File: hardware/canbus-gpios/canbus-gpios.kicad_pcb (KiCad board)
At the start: 4 copper layers, 55 x 35 mm, 34 parts, among them J1 USB_B_Micro, J2 UART, J3 10k NTC, J4 CANBus, J5 CANBus, J6 SWD, Q1 2N7002, Q2 2N7002, U1 MCP1754S-3302xCB, U2 STM32F042F6Px, U3 Voltage Regulator, U4 MCP2562HD

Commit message: Updated canbus-gpios to do GPIOs
- START_RUN and IGNITION_SENSE are active high 12V.
- EMERGENCY_STOP is active low 12V.
- all GPIOs converted to active high 3.3V at the CPU
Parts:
- added Q3: 2N7002, Package_TO_SOT_SMD:SOT-23, B.Cu at (100.4, 84.8)
- added Q4: 2N7002, Package_TO_SOT_SMD:SOT-23, B.Cu at (100.3, 81.3)
- added Q5: 2N7002, Package_TO_SOT_SMD:SOT-23, B.Cu at (100.3, 77.7)
- added R10: 10k, Resistor_SMD:R_0805_2012Metric_Pad1.20x1.40mm_HandSolder, B.Cu at (104.5, 75.0)
- added R8: 10k, Resistor_SMD:R_0805_2012Metric_Pad1.20x1.40mm_HandSolder, B.Cu at (100.9, 87.8)
- added R9: 10k, Resistor_SMD:R_0805_2012Metric_Pad1.20x1.40mm_HandSolder, B.Cu at (107.3, 80.2)
- J3: value 10k NTC -> GPIO; footprint TerminalBlock_TE-Connectivity:TerminalBlock_TE_282834-2_1x02_P2.54mm_Horizontal -> TerminalBlock_TE-Connectivity:TerminalBlock_TE_282834-3_1x03_P2.54mm_Horizontal
- R3: value 499k 1% -> 10k
- R4: value 100k 1% -> 10k
- moved R7 19.6 mm to (83.8, 81.8)
- moved R3 9.86 mm to (88.2, 81.8), turned to 90 degrees
- moved R4 6.00 mm to (86.0, 81.8), turned to 90 degrees
- moved J3 1.77 mm to (104.5, 78.8), turned to -90 degrees
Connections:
- J3 pad 1: VTHERM -> START_RUN
- J3 pad 2: GND -> IGNITION_SENSE
- R3 pad 1: +12V -> EMERGENCY_STOP_3V
- R3 pad 2: VBAT_MON -> +3V3
- R4 pad 1: VBAT_MON -> IGNITION_SENSE_3V
- R4 pad 2: GND -> +3V3
- R7 pad 1: +3V3 -> START_RUN_3V
- R7 pad 2: VTHERM -> +3V3
- U2 pad 10: ~{SPI1_SS} -> EMERGENCY_STOP_3V
- U2 pad 11: SPI1_SCK -> unconnected-(U2-Pad11)
- U2 pad 12: SPI1_MISO -> unconnected-(U2-Pad12)
- U2 pad 13: SPI1_MOSI -> unconnected-(U2-Pad13)
- U2 pad 6: VTHERM -> START_RUN_3V
- U2 pad 7: VBAT_MON -> IGNITION_SENSE_3V
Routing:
- net START_RUN_3V: track 0.00 -> 30.5 mm, vias 0 -> 2
- net +12V: track 14.4 -> 42.9 mm, vias 0 -> 1
- net VTHERM: track 25.1 -> 0.00 mm, vias 1 -> 0
- net IGNITION_SENSE_3V: track 0.00 -> 24.6 mm, vias 0 -> 2
- net EMERGENCY_STOP_3V: track 0.00 -> 18.3 mm, vias 0 -> 2
- net VBAT_MON: track 17.4 -> 0.00 mm, vias 2 -> 0
- net ~{EMERGENCY_STOP}: track 0.00 -> 8.18 mm
- net +3V3: track 22.3 -> 30.2 mm, vias 6 -> 8
- net START_RUN: track 0.00 -> 6.44 mm
- net IGNITION_SENSE: track 0.00 -> 6.07 mm
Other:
- board text added: "CANBus GPIO"
- board text removed: "CANBus Thermistor"

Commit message: Updated canbus-ds1820 board, reannotated canbus-gpios
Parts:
- renumbered J6 to J2, J2 to J3, J3 to J6, R6 to R10, R5 to R3, R3 to R4, R4 to R5, R7 to R6, R8 to R7, R9 to R8, R10 to R9
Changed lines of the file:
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@@
   (net 9 "USB_D+")
   (net 10 "unconnected-(J1-Pad4)")
-  (net 11 "Net-(J2-Pad4)")
+  (net 11 "unconnected-(J3-Pad1)")
   (net 12 "CANH")
   (net 13 "CANL")
@@
   (net 30 "SWDCLK")
   (net 31 "~{RESET}")
-  (net 32 "unconnected-(J2-Pad1)")
+  (net 32 "Net-(J3-Pad4)")
   (net 33 "START_RUN_3V")
-  (net 34 "unconnected-(J2-Pad5)")
+  (net 34 "unconnected-(J3-Pad5)")
   (net 35 "unconnected-(U3-Pad4)")
   (net 36 "/VDDA")
@@
     (property "Sheetname" "")
     (attr through_hole)
-    (fp_text reference "J6" (at 2.75 0.04 180) (layer "F.SilkS")
+    (fp_text reference "J2" (at 2.75 0.04 180) (layer "F.SilkS")
       (effects (font (size 1 1) (thickness 0.15)))
     )
@@
     (property "Sheetname" "")
     (attr smd)
-    (fp_text reference "R6" (at 2.8 0.025 180) (layer "F.SilkS")
+    (fp_text reference "R10" (at 2.8 0.025 180) (layer "F.SilkS")
       (effects (font (size 1 1) (thickness 0.15)))
     )
@@
     (property "Sheetname" "")
     (attr smd)
-    (fp_text reference "R5" (at -0.3 1.875 180) (layer "F.SilkS")
+    (fp_text reference "R3" (at -0.3 1.875 180) (layer "F.SilkS")
       (effects (font (size 1 1) (thickness 0.15)))
     )
@@
     (property "Sheetname" "")
     (attr exclude_from_pos_files)
-    (fp_text reference "J2" (at 15.11 -1.15) (layer "F.SilkS")
+    (fp_text reference "J3" (at 15.11 -1.15) (layer "F.SilkS")
       (effects (font (size 1.27 1.27) (thickness 0.127)))
     )
@@
     (fp_rect (start -1.2954 -1.3462) (end 13.97 1.3462) (layer "F.SilkS") (width 0.12) (fill none))
     (pad "1" thru_hole rect (at 0 0 270) (size 1.8796 1.8796) (drill 1.016) (layers *.Cu *.Paste *.Mask)
-      (net 32 "unconnected-(J2-Pad1)") (pinfunction "DTR") (pintype "passive+no_connect"))
+      (net 11 "unconnected-(J3-Pad1)") (pinfunction "DTR") (pintype "passive+no_connect"))
     (pad "2" thru_hole circle (at 2.54 0 270) (size 1.8796 1.8796) (drill 1.016) (layers *.Cu *.Paste *.Mask)
       (net 24 "RXD2") (pinfunction "RXD") (pintype "passive"))
@@
       (net 23 "TXD2") (pinfunction "TXD") (pintype "passive"))
     (pad "4" thru_hole circle (at 7.62 0 270) (size 1.8796 1.8796) (drill 1.016) (layers *.Cu *.Paste *.Mask)
-      (net 11 "Net-(J2-Pad4)") (pinfunction "VCC") (pintype "passive"))
+      (net 32 "Net-(J3-Pad4)") (pinfunction "VCC") (pintype "passive"))
     (pad "5" thru_hole circle (at 10.16 0 270) (size 1.8796 1.8796) (drill 1.016) (layers *.Cu *.Paste *.Mask)
-      (net 34 "unconnected-(J2-Pad5)") (pinfunction "CTS") (pintype "passive+no_connect"))
+      (net 34 "unconnected-(J3-Pad5)") (pinfunction "CTS") (pintype "passive+no_connect"))
     (pad "6" thru_hole circle (at 12.7 0 270) (size 1.8796 1.8796) (drill 1.016) (layers *.Cu *.Paste *.Mask)
       (net 1 "GND") (pinfunction "GND") (pintype "passive"))
@@
     (property "Sheetname" "")
     (attr through_hole)
-    (fp_text reference "J3" (at 7.875 0.475 180) (layer "F.SilkS")
+    (fp_text reference "J6" (at 7.875 0.475 180) (layer "F.SilkS")
       (effects (font (size 1 1) (thickness 0.15)))
     )
@@
     (fp_line (start 9.941268 35.017468) (end 44.941268 35.017468) (layer "Edge.Cuts") (width 0.15))
     (fp_arc (start 54.941268 25.017468) (mid 52.012336 32.088536) (end 44.941268 35.017468) (layer "Edge.Cuts") (width 0.15))
-    (fp_arc (start 9.941268 35.017468) (mid 2.870199 32.088536) (end -0.058732 25.017468) (layer "Edge.Cuts") (width 0.15))
-    (fp_arc (start 44.941268 0.017468) (mid 52.012338 2.946399) (end 54.941268 10.017468) (layer "Edge.Cuts") (width 0.15))
+    (fp_arc (start 9.941268 35.017468) (mid 2.8702 32.088536) (end -0.058732 25.017468) (layer "Edge.Cuts") (width 0.15))
+    (fp_arc (start 44.941268 0.017468) (mid 52.012334 2.9464) (end 54.941268 10.017468) (layer "Edge.Cuts") (width 0.15))
     (fp_arc (start -0.058732 10.017468) (mid 2.8702 2.9464) (end 9.941268 0.017468) (layer "Edge.Cuts") (width 0.15))
   )
@@
     (property "Sheetname" "")
     (attr smd)
-    (fp_text reference "R10" (at -1.575 1.7 90) (layer "B.SilkS")
+    (fp_text reference "R9" (at -1.575 1.7 90) (layer "B.SilkS")
       (effects (font (size 1 1) (thickness 0.15)) (justify mirror))
     )
@@
     (property "Sheetname" "")
     (attr smd)
-    (fp_text reference "R4" (at 3.175 0.075 90) (layer "B.SilkS")
+    (fp_text reference "R5" (at 3.175 0.075 90) (layer "B.SilkS")
       (effects (font (size 1 1) (thickness 0.15)) (justify mirror))
     )
@@
     (property "Sheetname" "")
     (attr smd)
-    (fp_text reference "R9" (at -3.2 0 90) (layer "B.SilkS")
+    (fp_text reference "R8" (at -3.2 0 90) (layer "B.SilkS")
       (effects (font (size 1 1) (thickness 0.15)) (justify mirror))
     )
@@
     (property "Sheetname" "")
     (attr smd)
-    (fp_text reference "R3" (at 3.2 0.1 90) (layer "B.SilkS")
+    (fp_text reference "R4" (at 3.2 0.1 90) (layer "B.SilkS")
       (effects (font (size 1 1) (thickness 0.15)) (justify mirror))
     )
@@
     (property "Sheetname" "")
     (attr smd)
-    (fp_text reference "R7" (at 3.2 0.175 90) (layer "B.SilkS")
+    (fp_text reference "R6" (at 3.2 0.175 90) (layer "B.SilkS")
       (effects (font (size 1 1) (thickness 0.15)) (justify mirror))
     )
@@
     (fp_line (start 1.65 -1.25) (end 1.65 1.25) (layer "B.CrtYd") (width 0.05))
     (pad "1" smd custom (at -0.725 0 270) (size 0.3 0.3) (layers "B.Cu" "B.Mask")
-      (net 11 "Net-(J2-Pad4)") (pinfunction "A") (pintype "passive") (zone_connect 2)
+      (net 32 "Net-(J3-Pad4)") (pinfunction "A") (pintype "passive") (zone_connect 2)
       (options (clearance outline) (anchor rect))
       (primitives
@@
     (property "Sheetname" "")
     (attr smd)
-    (fp_text reference "R8" (at -3.375 -0.05) (layer "B.SilkS")
+    (fp_text reference "R7" (at -3.375 -0.05) (layer "B.SilkS")
       (effects (font (size 1 1) (thickness 0.15)) (justify mirror))
     )
@@
   (segment (start 70.925 93.35) (end 74.5 93.35) (width 0.2) (layer "In1.Cu") (net 9))
   (segment (start 74.5 93.35) (end 75.505 92.345) (width 0.2) (layer "In1.Cu") (net 9))
-  (segment (start 93.565 78.61) (end 96.5 78.61) (width 0.25) (layer "B.Cu") (net 11))
-  (segment (start 93.475 78.7) (end 93.565 78.61) (width 0.25) (layer "B.Cu") (net 11))
   (segment (start 65.7 87.2) (end 65.7 89) (width 0.25) (layer "F.Cu") (net 12))
   (segment (start 65.7 89) (end 62.165 92.535) (width 0.25) (layer "F.Cu") (net 12))
@@
   (segment (start 99.4382 90.325) (end 99.4394 90.3238) (width 0.25) (layer "B.Cu") (net 31))
   (segment (start 97 90.325) (end 99.4382 90.325) (width 0.25) (layer "B.Cu") (net 31))
+  (segment (start 93.565 78.61) (end 96.5 78.61) (width 0.25) (layer "B.Cu") (net 32))
+  (segment (start 93.475 78.7) (end 93.565 78.61) (width 0.25) (layer "B.Cu") (net 32))
   (segment (start 83.725 85.475) (end 83.725 84.275) (width 0.25) (layer "F.Cu") (net 33))
   (segment (start 83.725 84.275) (end 83.775 84.225) (width 0.25) (layer "F.Cu") (net 33))

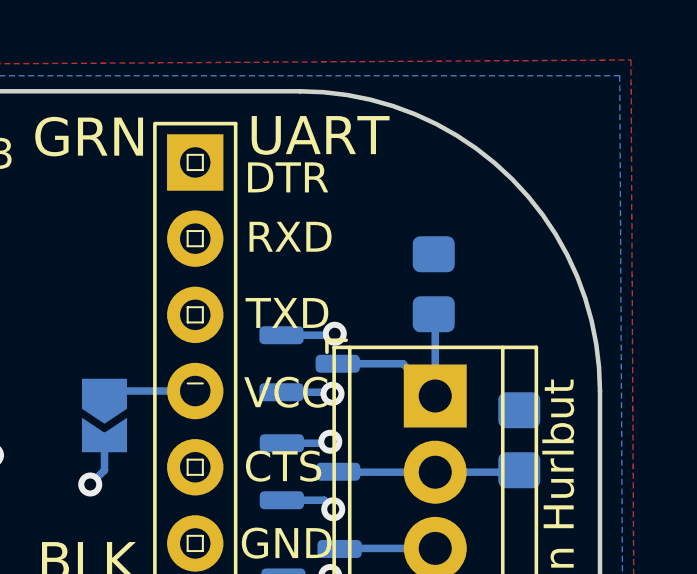
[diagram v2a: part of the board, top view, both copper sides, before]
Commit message: Updated the thermocouple board, added OSHW to bottom of all boards
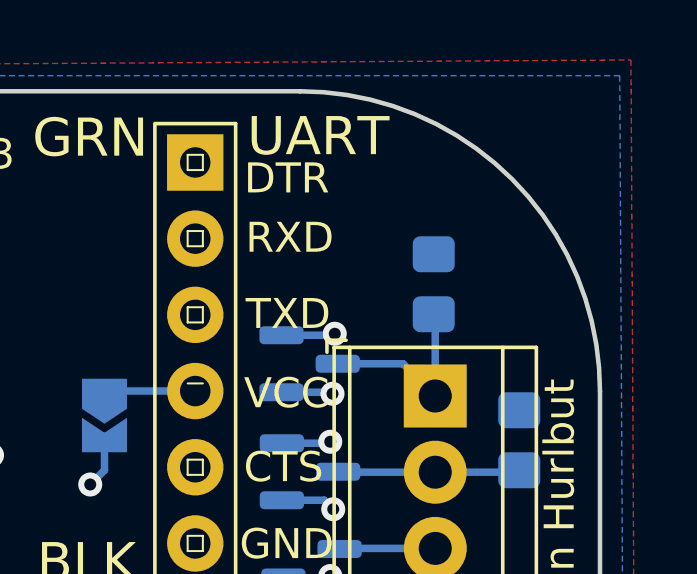
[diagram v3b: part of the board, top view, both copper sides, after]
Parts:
- added REF**: OSHW-Logo2_7.3x6mm_SilkScreen, Symbol:OSHW-Logo2_7.3x6mm_SilkScreen, B.Cu at (83.6, 74.2)
